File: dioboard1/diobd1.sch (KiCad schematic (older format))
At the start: 2 parts

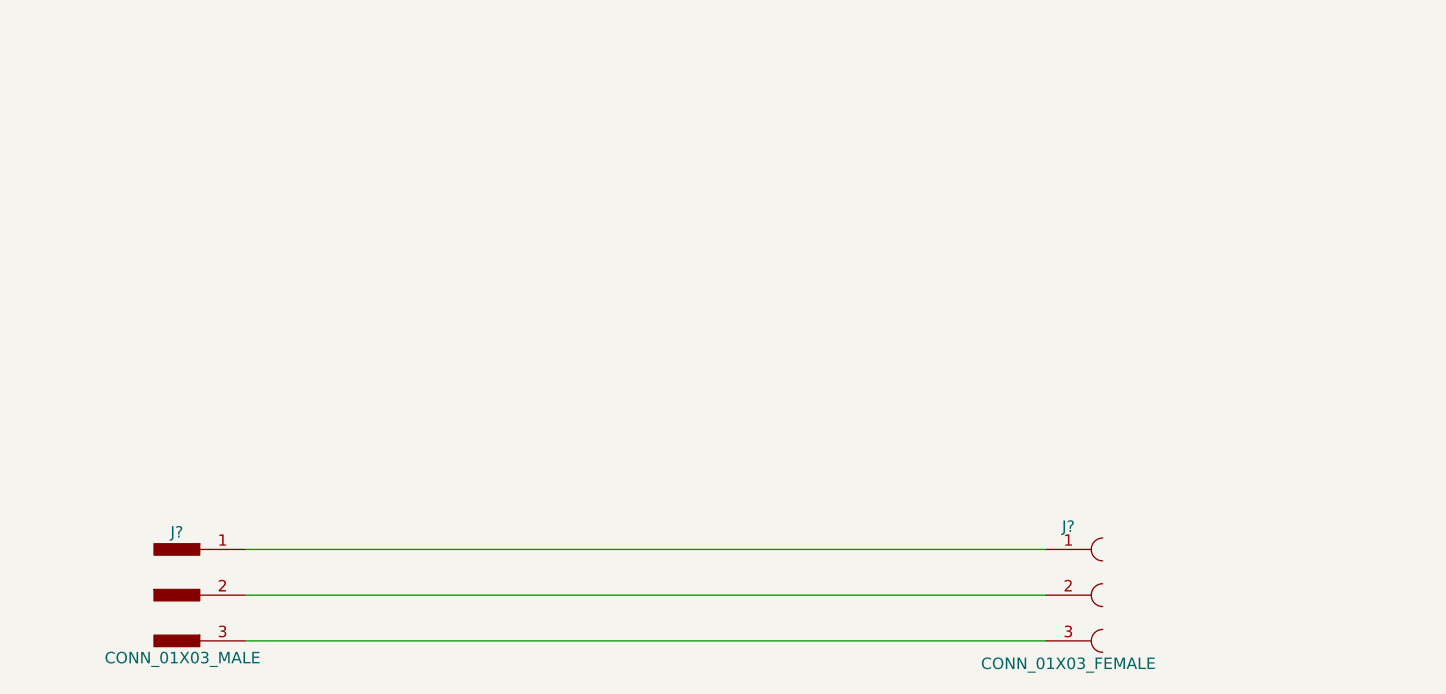
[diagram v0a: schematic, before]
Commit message: schematic edits. use power symbols.  add one LED circuit library for our own symbols
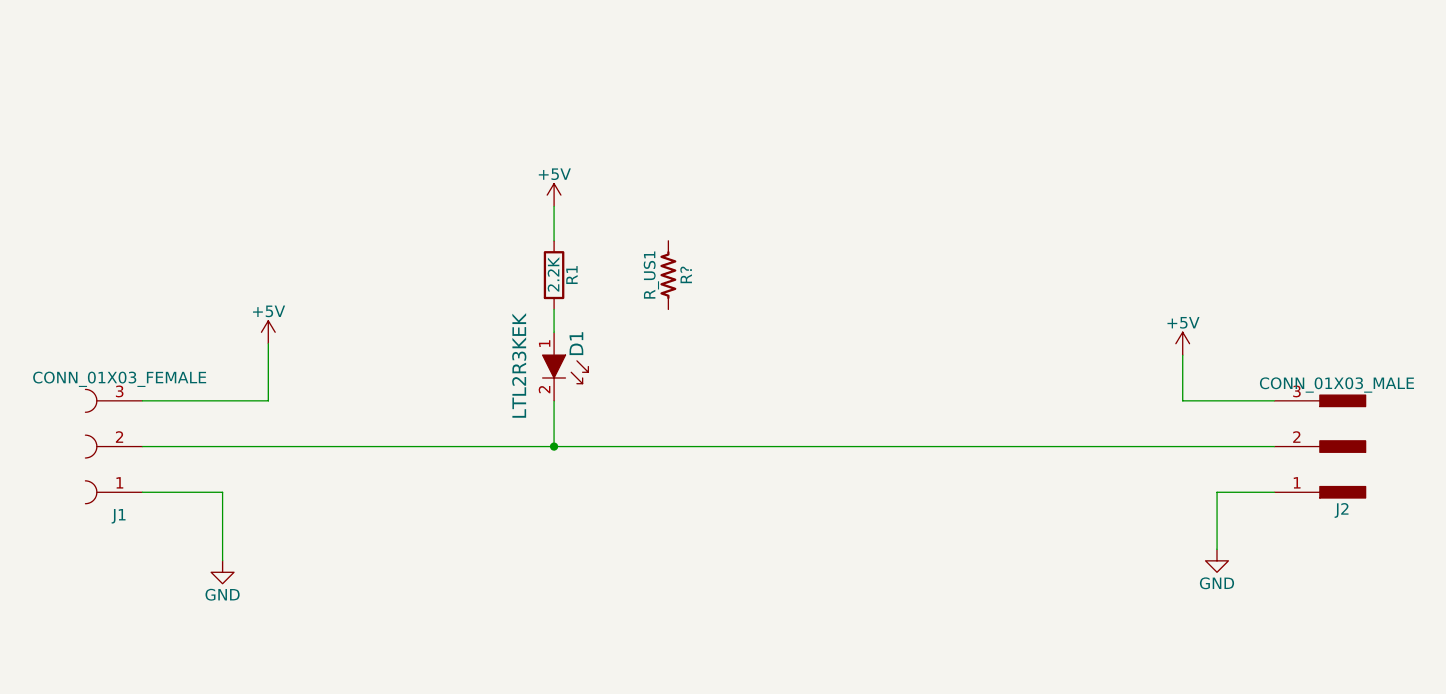
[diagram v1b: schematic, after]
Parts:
- added D1: LTL2R3KEK, LEDs:LED_D5.0mm, symbol LTL2R3KEK
- added R1: 2.2K, Resistors_THT:R_Axial_DIN0207_L6.3mm_D2.5mm_P10.16mm_Horizontal, symbol R
- added R?: R_US1, symbol R_US1
- J1: renamed from J?; footprint (none) -> Socket_Strips:Socket_Strip_Angled_1x03_Pitch2.54mm
- J2: renamed from J?; footprint (none) -> Pin_Headers:Pin_Header_Angled_1x03_Pitch2.54mm
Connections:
- net GND: now reaches J1.1, J2.1
- net at J1.2, J2.2: now also D1.2
- net +5V: now reaches J1.3, J2.3
- net +5V: now also R1.1
- new net: D1.1, R1.2
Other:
- moved on the sheet: J1, J2
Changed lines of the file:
@@
 LIBS:contrib
 LIBS:valves
+LIBS:dioboard1sym
 LIBS:diobd1-cache
 EELAYER 25 0
@@
 $EndDescr
 $Comp
-L CONN_01X03_FEMALE J?
+L CONN_01X03_FEMALE J1
 U 1 1 5BD283AF
-P 6600 3300
-F 0 "J?" H 6600 3600 50  0000 C CNN
-F 1 "CONN_01X03_FEMALE" H 6600 3000 50  0000 C CNN
-F 2 "" H 6600 3500 50  0001 C CNN
-F 3 "" H 6600 3500 50  0001 C CNN
-	1    6600 3300
+P 2450 2650
+F 0 "J1" H 2450 2950 50  0000 C CNN
+F 1 "CONN_01X03_FEMALE" H 2450 2350 50  0000 C CNN
+F 2 "Socket_Strips:Socket_Strip_Angled_1x03_Pitch2.54mm" H 2450 2850 50  0001 C CNN
+F 3 "" H 2450 2850 50  0001 C CNN
+	1    2450 2650
+	-1   0    0    1
+$EndComp
+$Comp
+L CONN_01X03_MALE J2
+U 1 1 5BD28790
+P 7800 2650
+F 0 "J2" H 7800 2925 50  0000 C CNN
+F 1 "CONN_01X03_MALE" H 7825 2375 50  0000 C CNN
+F 2 "Pin_Headers:Pin_Header_Angled_1x03_Pitch2.54mm" H 7800 2850 50  0001 C CNN
+F 3 "" H 7800 2850 50  0001 C CNN
+	1    7800 2650
+	-1   0    0    1
+$EndComp
+Wire Wire Line
+	2550 2450 3100 2450
+Wire Wire Line
+	2550 2650 7500 2650
+Wire Wire Line
+	2550 2850 2900 2850
+$Comp
+L GND #PWR01
+U 1 1 5BD52860
+P 2900 3150
+F 0 "#PWR01" H 2900 2900 50  0001 C CNN
+F 1 "GND" H 2900 3000 50  0000 C CNN
+F 2 "" H 2900 3150 50  0001 C CNN
+F 3 "" H 2900 3150 50  0001 C CNN
+	1    2900 3150
 	1    0    0    -1
 $EndComp
 $Comp
-L CONN_01X03_MALE J?
-U 1 1 5BD28790
-P 2700 3300
-F 0 "J?" H 2700 3575 50  0000 C CNN
-F 1 "CONN_01X03_MALE" H 2725 3025 50  0000 C CNN
-F 2 "" H 2700 3500 50  0001 C CNN
-F 3 "" H 2700 3500 50  0001 C CNN
-	1    2700 3300
+L GND #PWR02
+U 1 1 5BD52878
+P 7250 3100
+F 0 "#PWR02" H 7250 2850 50  0001 C CNN
+F 1 "GND" H 7250 2950 50  0000 C CNN
+F 2 "" H 7250 3100 50  0001 C CNN
+F 3 "" H 7250 3100 50  0001 C CNN
+	1    7250 3100
+	1    0    0    -1
+$EndComp
+$Comp
+L +5V #PWR03
+U 1 1 5BD52894
+P 3100 2200
+F 0 "#PWR03" H 3100 2050 50  0001 C CNN
+F 1 "+5V" H 3100 2340 50  0000 C CNN
+F 2 "" H 3100 2200 50  0001 C CNN
+F 3 "" H 3100 2200 50  0001 C CNN
+	1    3100 2200
+	1    0    0    -1
+$EndComp
+$Comp
+L +5V #PWR04
+U 1 1 5BD528AC
+P 7100 2250
+F 0 "#PWR04" H 7100 2100 50  0001 C CNN
+F 1 "+5V" H 7100 2390 50  0000 C CNN
+F 2 "" H 7100 2250 50  0001 C CNN
+F 3 "" H 7100 2250 50  0001 C CNN
+	1    7100 2250
 	1    0    0    -1
 $EndComp
 Wire Wire Line
-	3000 3100 6500 3100
+	3100 2450 3100 2200
 Wire Wire Line
-	3000 3300 6500 3300
+	2900 2850 2900 3150
 Wire Wire Line
-	3000 3500 6500 3500
+	7500 2450 7100 2450
+Wire Wire Line
+	7100 2450 7100 2250
+Wire Wire Line
+	7500 2850 7250 2850
+Wire Wire Line
+	7250 2850 7250 3100
+$Comp
+L LTL2R3KEK D1
+U 1 1 5BD536AB
+P 4350 2350
+F 0 "D1" H 4200 2450 60  0000 C CNN
+F 1 "LTL2R3KEK" H 4300 2200 60  0000 C CNN
+F 2 "LEDs:LED_D5.0mm" H 4550 2550 60  0001 L CNN
+F 3 "http://optoelectronics.liteon.com/upload/download/DS-20-98-0286/LTL2R3KEK.pdf" H 4550 2650 60  0001 L CNN
+F 4 "160-1682-ND" H 4550 2750 60  0001 L CNN "Digi-Key_PN"
+F 5 "LTL2R3KEK" H 4550 2850 60  0001 L CNN "MPN"
+F 6 "Optoelectronics" H 4550 2950 60  0001 L CNN "Category"
+F 7 "LED Indication - Discrete" H 4550 3050 60  0001 L CNN "Family"
+F 8 "http://optoelectronics.liteon.com/upload/download/DS-20-98-0286/LTL2R3KEK.pdf" H 4550 3150 60  0001 L CNN "DK_Datasheet_Link"
+F 9 "/product-detail/en/lite-on-inc/LTL2R3KEK/160-1682-ND/573572" H 4550 3250 60  0001 L CNN "DK_Detail_Page"
+F 10 "LED RED CLEAR T-1 3/4 T/H" H 4550 3350 60  0001 L CNN "Description"
+F 11 "Lite-On Inc." H 4550 3450 60  0001 L CNN "Manufacturer"
+F 12 "Active" H 4550 3550 60  0001 L CNN "Status"
+	1    4350 2350
+	0    1    1    0
+$EndComp
+Wire Wire Line
+	4350 2450 4350 2650
+Connection ~ 4350 2650
+$Comp
+L R R1
+U 1 1 5BD5389A
+P 4350 1900
+F 0 "R1" V 4430 1900 50  0000 C CNN
+F 1 "2.2K" V 4350 1900 50  0000 C CNN
+F 2 "Resistors_THT:R_Axial_DIN0207_L6.3mm_D2.5mm_P10.16mm_Horizontal" V 4280 1900 50  0001 C CNN
+F 3 "" H 4350 1900 50  0001 C CNN
+	1    4350 1900
+	1    0    0    -1
+$EndComp
+$Comp
+L +5V #PWR05
+U 1 1 5BD53973
+P 4350 1600
+F 0 "#PWR05" H 4350 1450 50  0001 C CNN
+F 1 "+5V" H 4350 1740 50  0000 C CNN
+F 2 "" H 4350 1600 50  0001 C CNN
+F 3 "" H 4350 1600 50  0001 C CNN
+	1    4350 1600
+	1    0    0    -1
+$EndComp
+Wire Wire Line
+	4350 1600 4350 1750
+Wire Wire Line
+	4350 2050 4350 2150
+$Comp
+L R_US1 R?
+U 1 1 5BDBD0EB
+P 4850 1900
+F 0 "R?" V 4930 1900 50  0000 C CNN
+F 1 "R_US1" V 4770 1900 50  0000 C CNN
+F 2 "" H 4850 1900 60  0001 C CNN
+F 3 "" H 4850 1900 60  0001 C CNN
+	1    4850 1900
+	1    0    0    -1
+$EndComp
 $EndSCHEMATC

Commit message: redraw with KiCad 5.0.1
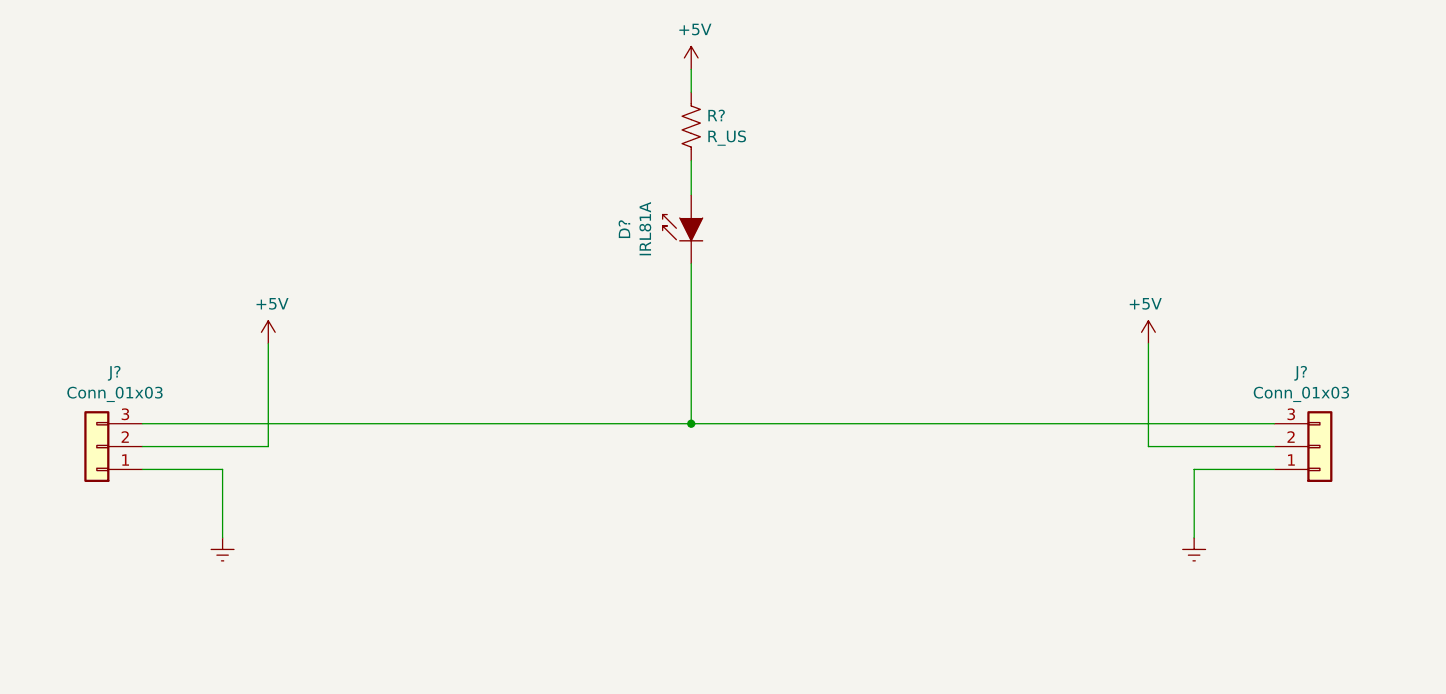
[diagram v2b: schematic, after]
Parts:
- removed D1: LTL2R3KEK, LEDs:LED_D5.0mm, symbol LTL2R3KEK
- removed J1: CONN_01X03_FEMALE, Socket_Strips:Socket_Strip_Angled_1x03_Pitch2.54mm, symbol CONN_01X03_FEMALE
- removed J2: CONN_01X03_MALE, Pin_Headers:Pin_Header_Angled_1x03_Pitch2.54mm, symbol CONN_01X03_MALE
- removed R1: 2.2K, Resistors_THT:R_Axial_DIN0207_L6.3mm_D2.5mm_P10.16mm_Horizontal, symbol R
- removed R?: R_US1, symbol R_US1
- added D?: IRL81A, LED_THT:LED_SideEmitter_Rectangular_W4.5mm_H1.6mm, symbol LED:IRL81A
- added J? (x2): Conn_01x03, symbol Connector_Generic:Conn_01x03
- added R?: R_US, symbol Device:R_US
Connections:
- net +5V: now also J?.2 (Pin_2), J?.2 (Pin_2), R?.1
- new net: D?.1 (K), J?.3 (Pin_3), J?.3 (Pin_3)
- new net: D?.2 (A), R?.2
- new net Earth: J?.1 (Pin_1), J?.1 (Pin_1)
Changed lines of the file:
@@
-EESchema Schematic File Version 2
+EESchema Schematic File Version 4
 LIBS:power
 LIBS:device
-LIBS:transistors
-LIBS:conn
-LIBS:linear
-LIBS:regul
 LIBS:74xx
-LIBS:cmos4000
-LIBS:adc-dac
-LIBS:memory
-LIBS:xilinx
-LIBS:microcontrollers
-LIBS:dsp
-LIBS:microchip
-LIBS:analog_switches
-LIBS:motorola
-LIBS:texas
-LIBS:intel
 LIBS:audio
 LIBS:interface
-LIBS:digital-audio
-LIBS:philips
-LIBS:display
-LIBS:cypress
-LIBS:siliconi
-LIBS:opto
-LIBS:atmel
-LIBS:contrib
-LIBS:valves
 LIBS:dioboard1sym
 LIBS:diobd1-cache
-EELAYER 25 0
+EELAYER 26 0
 EELAYER END
-$Descr A4 11693 8268
+$Descr USLetter 11000 8500
 encoding utf-8
 Sheet 1 1
-Title ""
-Date ""
-Rev ""
-Comp ""
+Title "DIO Breakout"
+Date "2018-11-02"
+Rev "3"
+Comp "Eastbots"
 Comment1 ""
 Comment2 ""
@@
 Comment4 ""
 $EndDescr
+Wire Wire Line
+	2550 2750 2900 2750
+Wire Wire Line
+	2900 2750 2900 3050
+Wire Wire Line
+	2550 2650 3100 2650
+Wire Wire Line
+	3100 2200 3100 2650
+Wire Wire Line
+	2550 2550 4950 2550
+Wire Wire Line
+	4950 1850 4950 2550
+Wire Wire Line
+	7500 2550 4950 2550
+Connection ~ 4950 2550
 $Comp
-L CONN_01X03_FEMALE J1
-U 1 1 5BD283AF
-P 2450 2650
-F 0 "J1" H 2450 2950 50  0000 C CNN
-F 1 "CONN_01X03_FEMALE" H 2450 2350 50  0000 C CNN
-F 2 "Socket_Strips:Socket_Strip_Angled_1x03_Pitch2.54mm" H 2450 2850 50  0001 C CNN
-F 3 "" H 2450 2850 50  0001 C CNN
-	1    2450 2650
+L LED:IRL81A D?
+U 1 1 5BDCCCDE
+P 4950 1650
+F 0 "D?" H 4900 1940 50  0000 C CNN
+F 1 "IRL81A" H 4900 1849 50  0000 C CNN
+F 2 "LED_THT:LED_SideEmitter_Rectangular_W4.5mm_H1.6mm" H 4950 1825 50  0001 C CNN
+F 3 "http://www.osram-os.com/Graphics/XPic0/00203825_0.pdf" H 4900 1650 50  0001 C CNN
+	1    4950 1650
+	0    -1   -1   0
+$EndComp
+$Comp
+L Device:R_US R?
+U 1 1 5BDCD126
+P 4950 1250
+F 0 "R?" H 5018 1296 50  0000 L CNN
+F 1 "R_US" H 5018 1205 50  0000 L CNN
+F 2 "" V 4990 1240 50  0001 C CNN
+F 3 "~" H 4950 1250 50  0001 C CNN
+	1    4950 1250
+	1    0    0    -1
+$EndComp
+$Comp
+L power:+5V #PWR?
+U 1 1 5BDCD7F2
+P 4950 1000
+F 0 "#PWR?" H 4950 850 50  0001 C CNN
+F 1 "+5V" H 4965 1173 50  0000 C CNN
+F 2 "" H 4950 1000 50  0001 C CNN
+F 3 "" H 4950 1000 50  0001 C CNN
+	1    4950 1000
+	1    0    0    -1
+$EndComp
+Wire Wire Line
+	4950 1100 4950 1000
+Wire Wire Line
+	4950 1550 4950 1400
+$Comp
+L Connector_Generic:Conn_01x03 J?
+U 1 1 5BDCDC09
+P 2350 2650
+F 0 "J?" H 2270 2325 50  0000 C CNN
+F 1 "Conn_01x03" H 2270 2416 50  0000 C CNN
+F 2 "" H 2350 2650 50  0001 C CNN
+F 3 "~" H 2350 2650 50  0001 C CNN
+	1    2350 2650
 	-1   0    0    1
 $EndComp
 $Comp
-L CONN_01X03_MALE J2
-U 1 1 5BD28790
-P 7800 2650
-F 0 "J2" H 7800 2925 50  0000 C CNN
-F 1 "CONN_01X03_MALE" H 7825 2375 50  0000 C CNN
-F 2 "Pin_Headers:Pin_Header_Angled_1x03_Pitch2.54mm" H 7800 2850 50  0001 C CNN
-F 3 "" H 7800 2850 50  0001 C CNN
-	1    7800 2650
-	-1   0    0    1
-$EndComp
-Wire Wire Line
-	2550 2450 3100 2450
-Wire Wire Line
-	2550 2650 7500 2650
-Wire Wire Line
-	2550 2850 2900 2850
-$Comp
-L GND #PWR01
-U 1 1 5BD52860
-P 2900 3150
-F 0 "#PWR01" H 2900 2900 50  0001 C CNN
-F 1 "GND" H 2900 3000 50  0000 C CNN
-F 2 "" H 2900 3150 50  0001 C CNN
-F 3 "" H 2900 3150 50  0001 C CNN
-	1    2900 3150
-	1    0    0    -1
-$EndComp
-$Comp
-L GND #PWR02
-U 1 1 5BD52878
-P 7250 3100
-F 0 "#PWR02" H 7250 2850 50  0001 C CNN
-F 1 "GND" H 7250 2950 50  0000 C CNN
-F 2 "" H 7250 3100 50  0001 C CNN
-F 3 "" H 7250 3100 50  0001 C CNN
-	1    7250 3100
-	1    0    0    -1
-$EndComp
-$Comp
-L +5V #PWR03
-U 1 1 5BD52894
+L power:+5V #PWR?
+U 1 1 5BDCDF40
 P 3100 2200
-F 0 "#PWR03" H 3100 2050 50  0001 C CNN
-F 1 "+5V" H 3100 2340 50  0000 C CNN
+F 0 "#PWR?" H 3100 2050 50  0001 C CNN
+F 1 "+5V" H 3115 2373 50  0000 C CNN
 F 2 "" H 3100 2200 50  0001 C CNN
 F 3 "" H 3100 2200 50  0001 C CNN
@@
 $EndComp
 $Comp
-L +5V #PWR04
-U 1 1 5BD528AC
-P 7100 2250
-F 0 "#PWR04" H 7100 2100 50  0001 C CNN
-F 1 "+5V" H 7100 2390 50  0000 C CNN
-F 2 "" H 7100 2250 50  0001 C CNN
-F 3 "" H 7100 2250 50  0001 C CNN
-	1    7100 2250
+L power:Earth #PWR?
+U 1 1 5BDCE0DF
+P 2900 3050
+F 0 "#PWR?" H 2900 2800 50  0001 C CNN
+F 1 "Earth" H 2900 2900 50  0001 C CNN
+F 2 "" H 2900 3050 50  0001 C CNN
+F 3 "~" H 2900 3050 50  0001 C CNN
+	1    2900 3050
 	1    0    0    -1
 $EndComp
 Wire Wire Line
-	3100 2450 3100 2200
+	7500 2750 7150 2750
 Wire Wire Line
-	2900 2850 2900 3150
+	7150 2750 7150 3050
 Wire Wire Line
-	7500 2450 7100 2450
+	7500 2650 6950 2650
 Wire Wire Line
-	7100 2450 7100 2250
-Wire Wire Line
-	7500 2850 7250 2850
-Wire Wire Line
-	7250 2850 7250 3100
+	6950 2200 6950 2650
 $Comp
-L LTL2R3KEK D1
-U 1 1 5BD536AB
-P 4350 2350
-F 0 "D1" H 4200 2450 60  0000 C CNN
-F 1 "LTL2R3KEK" H 4300 2200 60  0000 C CNN
-F 2 "LEDs:LED_D5.0mm" H 4550 2550 60  0001 L CNN
-F 3 "http://optoelectronics.liteon.com/upload/download/DS-20-98-0286/LTL2R3KEK.pdf" H 4550 2650 60  0001 L CNN
-F 4 "160-1682-ND" H 4550 2750 60  0001 L CNN "Digi-Key_PN"
-F 5 "LTL2R3KEK" H 4550 2850 60  0001 L CNN "MPN"
-F 6 "Optoelectronics" H 4550 2950 60  0001 L CNN "Category"
-F 7 "LED Indication - Discrete" H 4550 3050 60  0001 L CNN "Family"
-F 8 "http://optoelectronics.liteon.com/upload/download/DS-20-98-0286/LTL2R3KEK.pdf" H 4550 3150 60  0001 L CNN "DK_Datasheet_Link"
-F 9 "/product-detail/en/lite-on-inc/LTL2R3KEK/160-1682-ND/573572" H 4550 3250 60  0001 L CNN "DK_Detail_Page"
-F 10 "LED RED CLEAR T-1 3/4 T/H" H 4550 3350 60  0001 L CNN "Description"
-F 11 "Lite-On Inc." H 4550 3450 60  0001 L CNN "Manufacturer"
-F 12 "Active" H 4550 3550 60  0001 L CNN "Status"
-	1    4350 2350
-	0    1    1    0
-$EndComp
-Wire Wire Line
-	4350 2450 4350 2650
-Connection ~ 4350 2650
-$Comp
-L R R1
-U 1 1 5BD5389A
-P 4350 1900
-F 0 "R1" V 4430 1900 50  0000 C CNN
-F 1 "2.2K" V 4350 1900 50  0000 C CNN
-F 2 "Resistors_THT:R_Axial_DIN0207_L6.3mm_D2.5mm_P10.16mm_Horizontal" V 4280 1900 50  0001 C CNN
-F 3 "" H 4350 1900 50  0001 C CNN
-	1    4350 1900
-	1    0    0    -1
+L Connector_Generic:Conn_01x03 J?
+U 1 1 5BDCE519
+P 7700 2650
+F 0 "J?" H 7620 2325 50  0000 C CNN
+F 1 "Conn_01x03" H 7620 2416 50  0000 C CNN
+F 2 "" H 7700 2650 50  0001 C CNN
+F 3 "~" H 7700 2650 50  0001 C CNN
+	1    7700 2650
+	1    0    0    1
 $EndComp
 $Comp
-L +5V #PWR05
-U 1 1 5BD53973
-P 4350 1600
-F 0 "#PWR05" H 4350 1450 50  0001 C CNN
-F 1 "+5V" H 4350 1740 50  0000 C CNN
-F 2 "" H 4350 1600 50  0001 C CNN
-F 3 "" H 4350 1600 50  0001 C CNN
-	1    4350 1600
-	1    0    0    -1
+L power:+5V #PWR?
+U 1 1 5BDCE520
+P 6950 2200
+F 0 "#PWR?" H 6950 2050 50  0001 C CNN
+F 1 "+5V" H 6965 2373 50  0000 C CNN
+F 2 "" H 6950 2200 50  0001 C CNN
+F 3 "" H 6950 2200 50  0001 C CNN
+	1    6950 2200
+	-1   0    0    -1
 $EndComp
-Wire Wire Line
-	4350 1600 4350 1750
-Wire Wire Line
-	4350 2050 4350 2150
 $Comp
-L R_US1 R?
-U 1 1 5BDBD0EB
-P 4850 1900
-F 0 "R?" V 4930 1900 50  0000 C CNN
-F 1 "R_US1" V 4770 1900 50  0000 C CNN
-F 2 "" H 4850 1900 60  0001 C CNN
-F 3 "" H 4850 1900 60  0001 C CNN
-	1    4850 1900
-	1    0    0    -1
+L power:Earth #PWR?
+U 1 1 5BDCE526
+P 7150 3050
+F 0 "#PWR?" H 7150 2800 50  0001 C CNN
+F 1 "Earth" H 7150 2900 50  0001 C CNN
+F 2 "" H 7150 3050 50  0001 C CNN
+F 3 "~" H 7150 3050 50  0001 C CNN
+	1    7150 3050
+	-1   0    0    -1
 $EndComp
 $EndSCHEMATC
